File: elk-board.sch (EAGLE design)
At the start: 200 parts, among them IC1 KLM8G1GESD-B03P, IC10 MP2143DJ-LF-P, IC2 ALLWINNER--H3, IC3 SY6280, IC4 K4B4G1646D-BCK0, IC5 RT8059GJ5, IC6 RT8059GJ5, IC7 SY8089A, IC8 NCP803SN263T1G, IC9 RT8059GJ5, Q1 AO3415A, Q2 BCM856BS, Q3 9HT10-32.768KEZF-T, Q4 L2N7002WT1G, U1 AP6212, U2 STM32F411CEU6TR, X1 10118192-0001LF, Y1 26MHz, Y2 24MHz

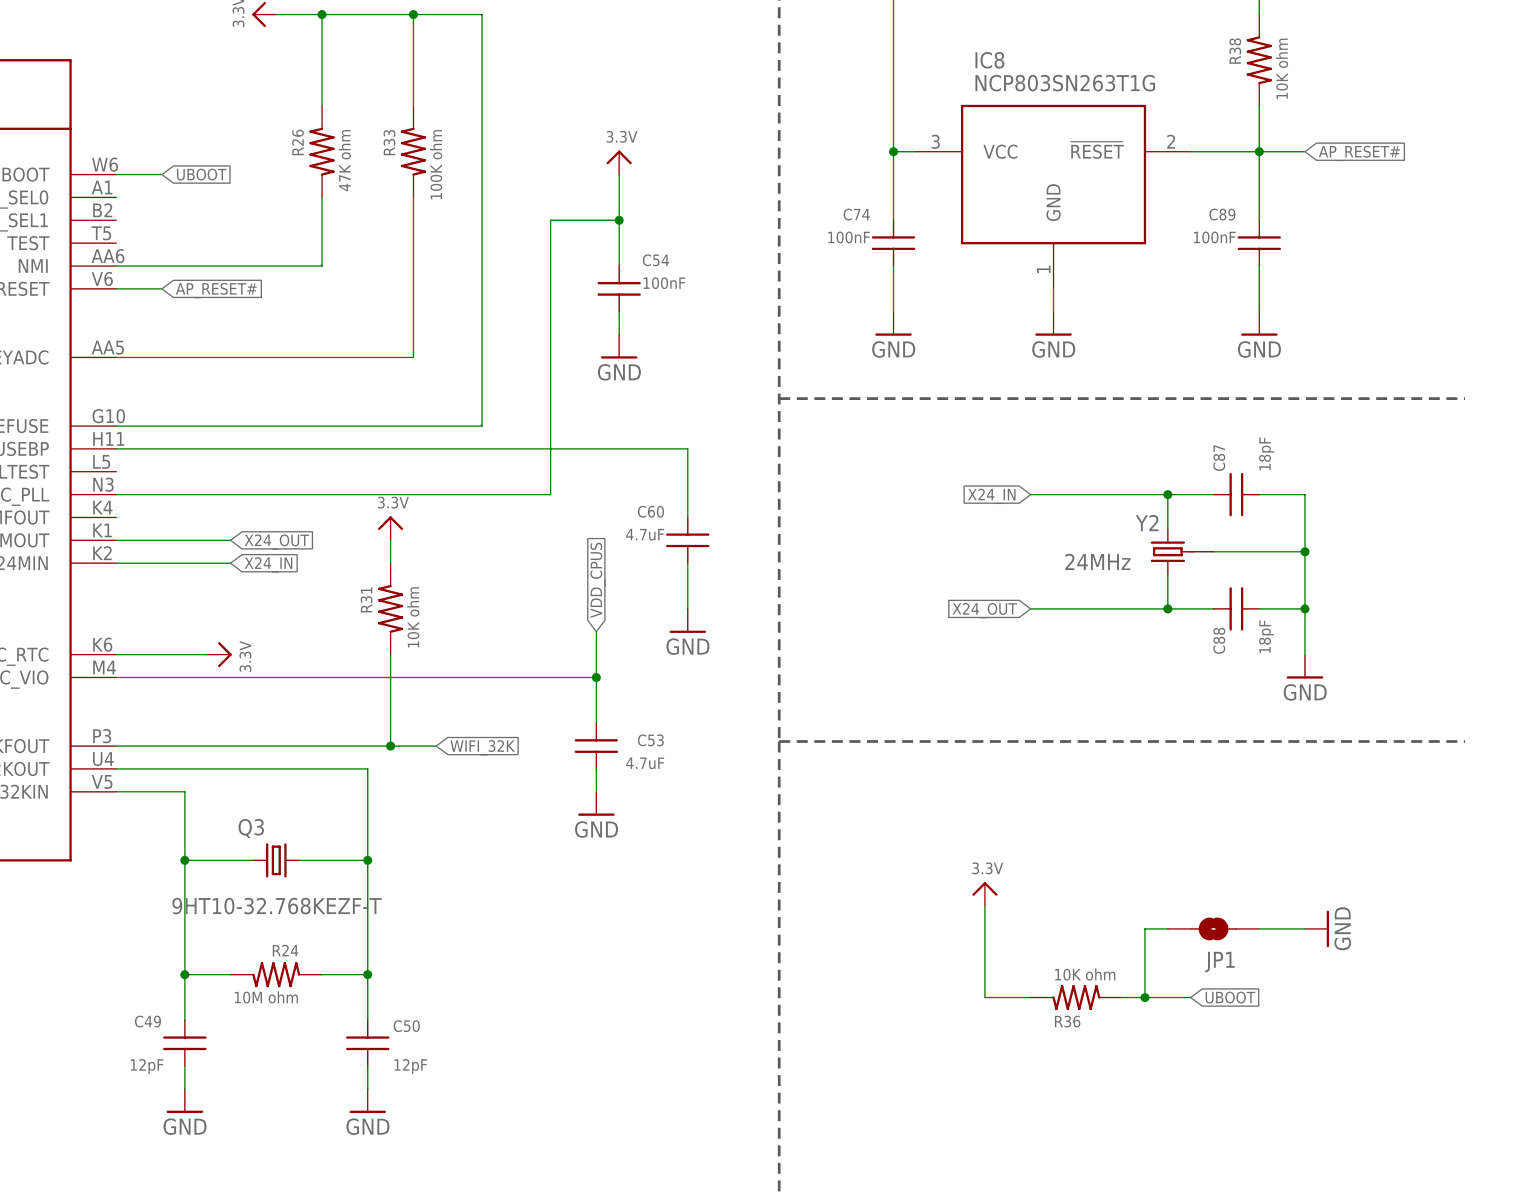
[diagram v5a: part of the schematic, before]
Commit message: CONNECT UBOOT WITH SETUP Button
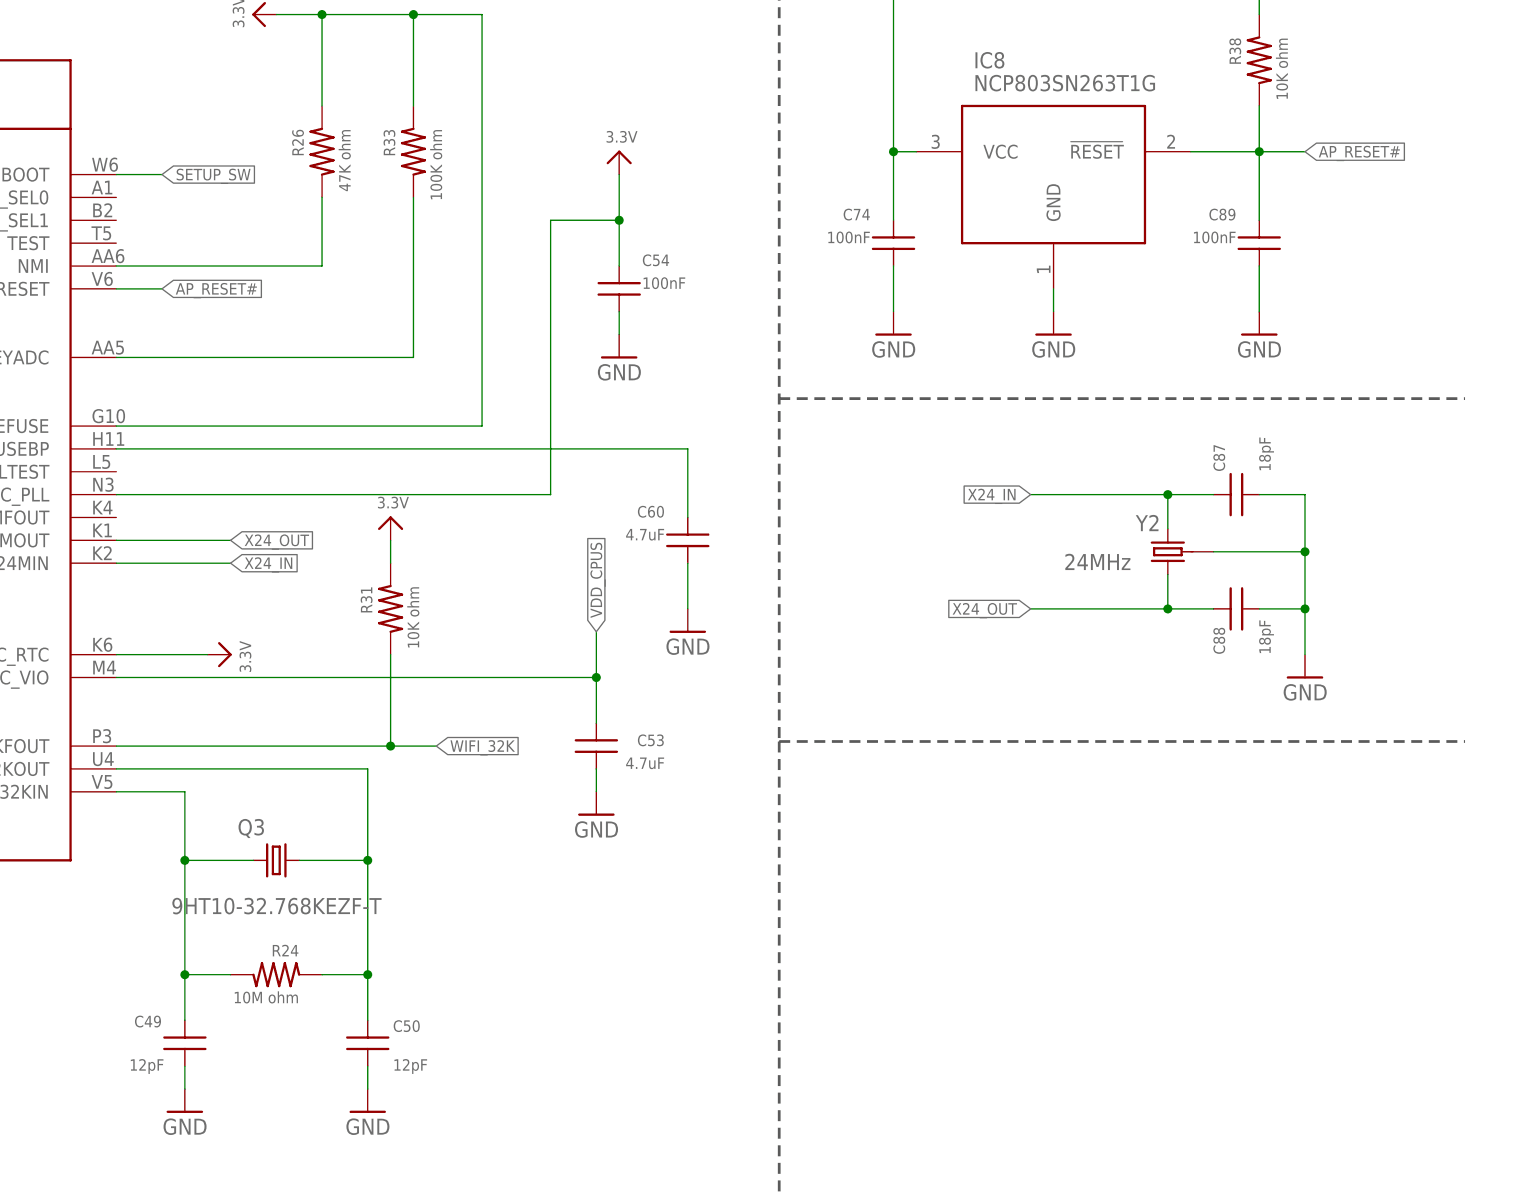
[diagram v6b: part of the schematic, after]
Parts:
- removed JP1: JUMPER-SMT_2_NO_SILK, SparkFun-Jumpers:JUMPER-SMT_2_NO_SILK
- removed R36: 10K ohm, GHI-BasicComponents:RESISTOR-(INCH)-0402
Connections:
- removed net UBOOT: IC2G$7.UBOOT, JP1.2, R36.2
- net 3.3V: no longer R36.1
- net GND: no longer JP1.1
- net SETUP_SW: now also IC2G$7.UBOOT
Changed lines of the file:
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@@
 <part name="R31" library="GHI-BasicComponents" deviceset="RESISTOR-(INCH)-" device="0402" value="10K ohm"/>
 <part name="3.3V17" library="microbuilder" deviceset="3.3V" device=""/>
-<part name="3.3V19" library="microbuilder" deviceset="3.3V" device=""/>
-<part name="R36" library="GHI-BasicComponents" deviceset="RESISTOR-(INCH)-" device="0402" value="10K ohm"/>
 <part name="GND95" library="supply1" deviceset="GND" device=""/>
 <part name="S2" library="Spark" deviceset="TAC_SWITCH" device="SMD" value="KMR231GLFS"/>
@@
 <part name="R52" library="GHI-BasicComponents" deviceset="RESISTOR-(INCH)-" device="0402" value="10K ohm"/>
 <part name="3.3V29" library="microbuilder" deviceset="3.3V" device=""/>
-<part name="GND74" library="supply1" library_urn="urn:adsk.eagle:library:371" deviceset="GND" device=""/>
-<part name="JP1" library="SparkFun-Jumpers" library_urn="urn:adsk.eagle:library:528" deviceset="JUMPER-SMT_2_NO" device="_SILK" package3d_urn="urn:adsk.eagle:package:39279/1" value="JUMPER-SMT_2_NO_SILK"/>
 <part name="C92" library="GHI-BasicComponents" deviceset="CAPACITOR-(INCH)-" device="0402" value="100nF"/>
 <part name="3.3V18" library="microbuilder" deviceset="3.3V" device=""/>
@@
 <attribute name="VALUE" x="399.796" y="465.836" size="1.27" layer="96"/>
 </instance>
-<instance part="3.3V19" gate="G$1" x="467.36" y="424.18" smashed="yes">
-<attribute name="VALUE" x="465.836" y="425.196" size="1.27" layer="96"/>
-</instance>
-<instance part="R36" gate="G$1" x="477.52" y="411.48" smashed="yes" rot="MR180">
-<attribute name="NAME" x="474.98" y="409.448" size="1.27" layer="95" font="vector" rot="MR180"/>
-<attribute name="VALUE" x="474.98" y="414.655" size="1.27" layer="96" font="vector" rot="MR180"/>
-</instance>
 <instance part="GND95" gate="1" x="723.9" y="764.54" smashed="yes">
 <attribute name="VALUE" x="721.36" y="762" size="1.778" layer="96"/>
@@
 <attribute name="VALUE" x="707.136" y="797.306" size="1.27" layer="96"/>
 </instance>
-<instance part="GND74" gate="1" x="505.46" y="419.1" smashed="yes" rot="MR270">
-<attribute name="VALUE" x="508" y="421.64" size="1.778" layer="96" rot="MR270"/>
-</instance>
-<instance part="JP1" gate="G$1" x="492.76" y="419.1" smashed="yes" rot="R180">
-<attribute name="NAME" x="495.3" y="416.56" size="1.778" layer="95" font="vector" rot="R180"/>
-</instance>
 <instance part="C92" gate="G$1" x="510.54" y="63.5" smashed="yes">
 <attribute name="NAME" x="513.08" y="66.04" size="1.27" layer="95" font="vector"/>
@@
 </segment>
 <segment>
-<pinref part="GND74" gate="1" pin="GND"/>
-<wire x1="497.84" y1="419.1" x2="502.92" y2="419.1" width="0.1524" layer="91"/>
-<pinref part="JP1" gate="G$1" pin="1"/>
-</segment>
-<segment>
 <pinref part="R37" gate="G$1" pin="2"/>
 <pinref part="GND70" gate="1" pin="GND"/>
@@
 </segment>
 <segment>
-<pinref part="3.3V19" gate="G$1" pin="3.3V"/>
-<wire x1="467.36" y1="421.64" x2="467.36" y2="411.48" width="0.1524" layer="91"/>
-<pinref part="R36" gate="G$1" pin="1"/>
-<wire x1="472.44" y1="411.48" x2="467.36" y2="411.48" width="0.1524" layer="91"/>
-</segment>
-<segment>
 <pinref part="IC2" gate="G$2" pin="EPHY_VCC"/>
 <wire x1="566.42" y1="388.62" x2="553.72" y2="388.62" width="0.1524" layer="91"/>
@@
 </segment>
 </net>
-<net name="UBOOT" class="0">
-<segment>
-<pinref part="IC2" gate="G$7" pin="UBOOT"/>
-<wire x1="370.84" y1="502.92" x2="375.92" y2="502.92" width="0.1524" layer="91"/>
-<label x="375.92" y="502.92" size="1.27" layer="95" xref="yes"/>
-</segment>
-<segment>
-<pinref part="R36" gate="G$1" pin="2"/>
-<wire x1="482.6" y1="411.48" x2="485.14" y2="411.48" width="0.1524" layer="91"/>
-<label x="490.22" y="411.48" size="1.27" layer="95" xref="yes"/>
-<pinref part="JP1" gate="G$1" pin="2"/>
-<wire x1="485.14" y1="411.48" x2="490.22" y2="411.48" width="0.1524" layer="91"/>
-<wire x1="487.68" y1="419.1" x2="485.14" y2="419.1" width="0.1524" layer="91"/>
-<wire x1="485.14" y1="419.1" x2="485.14" y2="411.48" width="0.1524" layer="91"/>
-<junction x="485.14" y="411.48"/>
-</segment>
-</net>
 <net name="AP_RESET#" class="0">
 <segment>
@@
 <net name="SETUP_SW" class="0">
 <segment>
+<pinref part="IC2" gate="G$1" pin="PA20/PCM0_DOUT/SIM_VPPEN/PA_EINT20"/>
+<wire x1="68.58" y1="462.28" x2="58.42" y2="462.28" width="0.1524" layer="91"/>
+<label x="58.42" y="462.28" size="1.27" layer="95" rot="R180" xref="yes"/>
+</segment>
+<segment>
+<pinref part="IC2" gate="G$7" pin="UBOOT"/>
+<wire x1="370.84" y1="502.92" x2="375.92" y2="502.92" width="0.1524" layer="91"/>
+<label x="375.92" y="502.92" size="1.27" layer="95" xref="yes"/>
+</segment>
+<segment>
 <wire x1="576.58" y1="754.38" x2="574.04" y2="754.38" width="0.1524" layer="91"/>
 <wire x1="574.04" y1="754.38" x2="566.42" y2="754.38" width="0.1524" layer="91"/>
@@
 <wire x1="574.04" y1="760.73" x2="574.04" y2="754.38" width="0.1524" layer="91"/>
 </segment>
-<segment>
-<pinref part="IC2" gate="G$1" pin="PA20/PCM0_DOUT/SIM_VPPEN/PA_EINT20"/>
-<wire x1="68.58" y1="462.28" x2="58.42" y2="462.28" width="0.1524" layer="91"/>
-<label x="58.42" y="462.28" size="1.27" layer="95" rot="R180" xref="yes"/>
-</segment>
 </net>

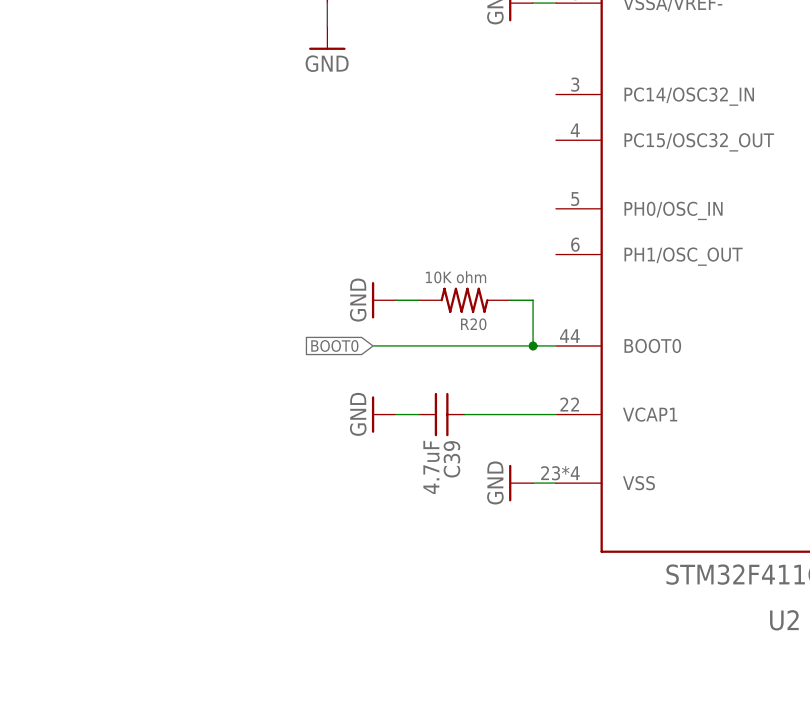
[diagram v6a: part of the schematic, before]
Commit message: Added External Oscillator to MCU Schematics
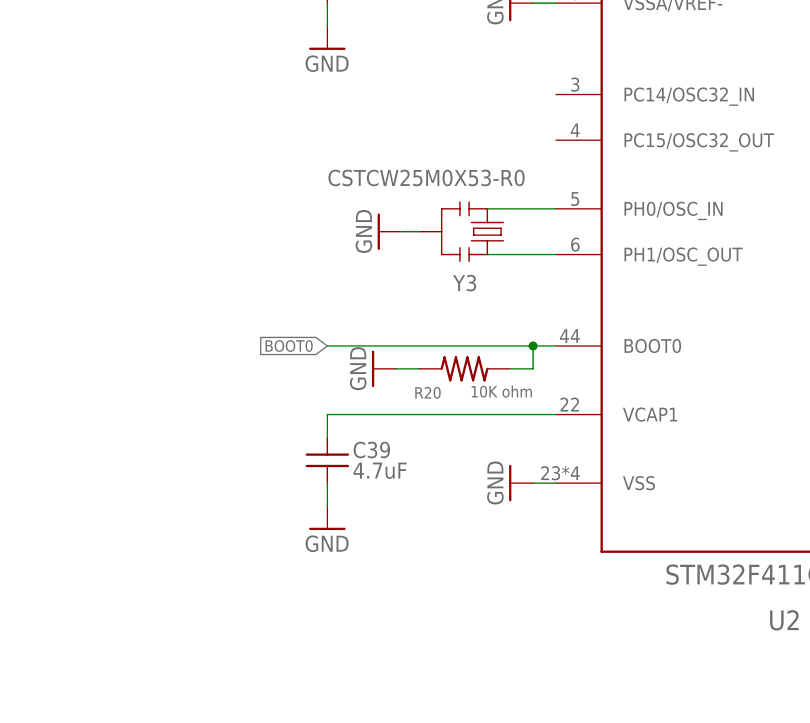
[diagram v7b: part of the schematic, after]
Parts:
- added Y3: CSTCW25M0X53-R0, Tolba_Resonators:CSTCW25M0X53-R0
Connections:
- new net N$15: U2.PH0/OSC_IN, Y3.IN
- new net N$16: U2.PH1/OSC_OUT, Y3.OUT
- net GND: now also Y3.GND
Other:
- moved on the sheet: C39, R20
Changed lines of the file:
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@@
 <part name="GND24" library="supply1" library_urn="urn:adsk.eagle:library:371" deviceset="GND" device=""/>
 <part name="GND98" library="supply1" deviceset="GND" device=""/>
+<part name="Y3" library="Tolba_Resonators" deviceset="CSTCW25M0X53-R0" device=""/>
+<part name="GND74" library="supply1" deviceset="GND" device=""/>
 </parts>
 <sheets>
@@
 <attribute name="VALUE" x="294.64" y="289.56" size="1.778" layer="96"/>
 </instance>
-<instance part="C39" gate="G$1" x="309.88" y="251.46" smashed="yes" rot="R270">
-<attribute name="NAME" x="310.134" y="248.666" size="1.778" layer="95" rot="R270"/>
-<attribute name="VALUE" x="307.848" y="248.666" size="1.778" layer="96" rot="R270"/>
+<instance part="C39" gate="G$1" x="297.18" y="246.38" smashed="yes">
+<attribute name="NAME" x="299.974" y="246.634" size="1.778" layer="95"/>
+<attribute name="VALUE" x="299.974" y="244.348" size="1.778" layer="96"/>
 </instance>
-<instance part="GND36" gate="1" x="302.26" y="251.46" smashed="yes" rot="R270">
-<attribute name="VALUE" x="299.72" y="254" size="1.778" layer="96" rot="R270"/>
+<instance part="GND36" gate="1" x="297.18" y="238.76" smashed="yes">
+<attribute name="VALUE" x="294.64" y="236.22" size="1.778" layer="96"/>
 </instance>
 <instance part="GND38" gate="1" x="317.5" y="243.84" smashed="yes" rot="R270">
@@
 <attribute name="VALUE" x="393.7" y="274.32" size="1.778" layer="96" rot="R90"/>
 </instance>
-<instance part="GND35" gate="1" x="302.26" y="264.16" smashed="yes" rot="R270">
-<attribute name="VALUE" x="299.72" y="266.7" size="1.778" layer="96" rot="R270"/>
+<instance part="GND35" gate="1" x="302.26" y="256.54" smashed="yes" rot="R270">
+<attribute name="VALUE" x="299.72" y="259.08" size="1.778" layer="96" rot="R270"/>
 </instance>
-<instance part="R20" gate="G$1" x="312.42" y="264.16" smashed="yes" rot="R180">
-<attribute name="NAME" x="314.96" y="262.128" size="1.27" layer="95" font="vector" rot="R180"/>
-<attribute name="VALUE" x="314.96" y="267.335" size="1.27" layer="96" font="vector" rot="R180"/>
+<instance part="R20" gate="G$1" x="312.42" y="256.54" smashed="yes" rot="R180">
+<attribute name="NAME" x="309.88" y="254.508" size="1.27" layer="95" font="vector" rot="R180"/>
+<attribute name="VALUE" x="320.04" y="254.635" size="1.27" layer="96" font="vector" rot="R180"/>
 </instance>
 <instance part="LED4" gate="G$1" x="584.2" y="792.48" smashed="yes">
@@
 <attribute name="VALUE" x="350.52" y="802.005" size="1.778" layer="96"/>
 </instance>
+<instance part="Y3" gate="G$1" x="312.42" y="271.78" smashed="yes" rot="R270">
+<attribute name="NAME" x="311.15" y="265.176" size="1.778" layer="95"/>
+<attribute name="VALUE" x="297.18" y="276.86" size="1.778" layer="96"/>
+</instance>
+<instance part="GND74" gate="1" x="302.895" y="271.78" smashed="yes" rot="R270">
+<attribute name="VALUE" x="300.355" y="274.32" size="1.778" layer="96" rot="R270"/>
+</instance>
 </instances>
 <busses>
@@
 <pinref part="C39" gate="G$1" pin="P$2"/>
 <pinref part="GND36" gate="1" pin="GND"/>
-<wire x1="307.34" y1="251.46" x2="304.8" y2="251.46" width="0.1524" layer="91"/>
+<wire x1="297.18" y1="243.84" x2="297.18" y2="241.3" width="0.1524" layer="91"/>
 </segment>
 <segment>
@@
 <pinref part="GND35" gate="1" pin="GND"/>
 <pinref part="R20" gate="G$1" pin="2"/>
-<wire x1="304.8" y1="264.16" x2="307.34" y2="264.16" width="0.1524" layer="91"/>
+<wire x1="304.8" y1="256.54" x2="307.34" y2="256.54" width="0.1524" layer="91"/>
 </segment>
 <segment>
@@
 <wire x1="353.06" y1="807.085" x2="353.06" y2="810.26" width="0.1524" layer="91"/>
 </segment>
+<segment>
+<pinref part="Y3" gate="G$1" pin="GND"/>
+<pinref part="GND74" gate="1" pin="GND"/>
+<wire x1="307.34" y1="271.78" x2="305.435" y2="271.78" width="0.1524" layer="91"/>
+</segment>
 </net>
 <net name="N$1" class="9">
@@
 <net name="N$22" class="0">
 <segment>
-<wire x1="322.58" y1="251.46" x2="312.42" y2="251.46" width="0.1524" layer="91"/>
+<wire x1="322.58" y1="251.46" x2="297.18" y2="251.46" width="0.1524" layer="91"/>
+<wire x1="297.18" y1="251.46" x2="297.18" y2="248.92" width="0.1524" layer="91"/>
 <pinref part="C39" gate="G$1" pin="P$1"/>
 <pinref part="U2" gate="G$1" pin="VCAP1"/>
@@
 <pinref part="U2" gate="G$1" pin="BOOT0"/>
 <pinref part="R20" gate="G$1" pin="1"/>
-<wire x1="317.5" y1="264.16" x2="320.04" y2="264.16" width="0.1524" layer="91"/>
-<wire x1="320.04" y1="264.16" x2="320.04" y2="259.08" width="0.1524" layer="91"/>
-<label x="302.26" y="259.08" size="1.27" layer="95" rot="R180" xref="yes"/>
-<wire x1="320.04" y1="259.08" x2="302.26" y2="259.08" width="0.1524" layer="91"/>
+<wire x1="317.5" y1="256.54" x2="320.04" y2="256.54" width="0.1524" layer="91"/>
+<wire x1="320.04" y1="256.54" x2="320.04" y2="259.08" width="0.1524" layer="91"/>
+<label x="297.18" y="259.08" size="1.27" layer="95" rot="R180" xref="yes"/>
+<wire x1="320.04" y1="259.08" x2="297.18" y2="259.08" width="0.1524" layer="91"/>
 <junction x="320.04" y="259.08"/>
 </segment>
@@
 </segment>
 </net>
+<net name="N$15" class="0">
+<segment>
+<pinref part="Y3" gate="G$1" pin="IN"/>
+<pinref part="U2" gate="G$1" pin="PH0/OSC_IN"/>
+<wire x1="314.96" y1="274.32" x2="322.58" y2="274.32" width="0.1524" layer="91"/>
+</segment>
+</net>
+<net name="N$16" class="0">
+<segment>
+<pinref part="U2" gate="G$1" pin="PH1/OSC_OUT"/>
+<pinref part="Y3" gate="G$1" pin="OUT"/>
+<wire x1="322.58" y1="269.24" x2="314.96" y2="269.24" width="0.1524" layer="91"/>
+</segment>
+</net>
